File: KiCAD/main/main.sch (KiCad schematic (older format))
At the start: 14 parts, among them IC1 DHT22, J1 Charge controller, J2 Sound Sensor, J3 BuckConverter, J4 Anemometer, Q1 Q_NJFET_DGS, U1 4020, U1 4N25, U2 4N25

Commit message: alimentação através do micro
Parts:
- removed Q1: Q_NJFET_DGS, symbol Device:Q_NJFET_DGS
- removed R1: 1k, symbol Device:R
- removed R? (x2): R, Resistor_SMD:R_1206_3216Metric, symbol Device:R
- removed U2: 4N25, Package_DIP:DIP-6_W7.62mm, symbol Isolator:4N25
- added SW?: SW_DPDT_x2, symbol Switch:SW_DPDT_x2
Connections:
- net VDD_on is gone; now on net supply_on: IC1.1 (VDD), J2.3 (Pin_3)
- net Vin_Buck: now also SW?.1 (A); no longer J1.1 (Pin_1)
- new net: J1.1 (Pin_1), SW?.2 (B)
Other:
- moved on the sheet: IC1, J4
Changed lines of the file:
@@
 Text Label 2900 3450 2    50   ~ 0
 DHT22_Data
-Text Label 1550 2700 0    50   ~ 0
+Text Label 2450 2400 0    50   ~ 0
 Vin_Buck
 Text Label 1550 2800 0    50   ~ 0
@@
 	4750 2650 4450 2650
 Wire Wire Line
-	9100 2950 9500 2950
-Wire Wire Line
-	1200 3900 1500 3900
+	9250 2700 9650 2700
 $Comp
 L Connector_Generic:Conn_01x04 J3
@@
 	1200 1750 1500 1750
 Wire Wire Line
-	1550 2700 1250 2700
-Wire Wire Line
 	1550 2800 1250 2800
 $Comp
 L Connector_Generic:Conn_01x02 J4
 U 1 1 5FC61584
-P 9700 2850
-F 0 "J4" H 9780 2842 50  0000 L CNN
-F 1 "Anemometer" H 9780 2751 50  0000 L CNN
-F 2 "Connector_JST:JST_PH_B2B-PH-K_1x02_P2.00mm_Vertical" H 9700 2850 50  0001 C CNN
-F 3 "~" H 9700 2850 50  0001 C CNN
-	1    9700 2850
-	1    0    0    -1
-$EndComp
-Text Label 8800 4400 2    50   ~ 0
-GND
-Text Label 8800 4200 2    50   ~ 0
+P 9850 2600
+F 0 "J4" H 9930 2592 50  0000 L CNN
+F 1 "Anemometer" H 9930 2501 50  0000 L CNN
+F 2 "Connector_JST:JST_PH_B2B-PH-K_1x02_P2.00mm_Vertical" H 9850 2600 50  0001 C CNN
+F 3 "~" H 9850 2600 50  0001 C CNN
+	1    9850 2600
+	1    0    0    -1
+$EndComp
+Text Label 8150 3900 2    50   ~ 0
+GND
+Text Label 8150 3700 2    50   ~ 0
 DHT22_Data
 Wire Wire Line
-	9000 4300 8900 4300
-NoConn ~ 8900 4300
-Wire Wire Line
-	9000 4400 8800 4400
-Wire Wire Line
-	9000 4200 8800 4200
+	8350 3800 8250 3800
+NoConn ~ 8250 3800
+Wire Wire Line
+	8350 3900 8150 3900
+Wire Wire Line
+	8350 3700 8150 3700
 $Comp
 L DHT22:DHT22 IC1
 U 1 1 5FB3BE3A
-P 9000 4100
-F 0 "IC1" H 9342 3535 50  0000 C CNN
-F 1 "DHT22" H 9342 3626 50  0000 C CNN
-F 2 "DHT22" H 9750 4200 50  0001 L CNN
-F 3 "https://datasheet4u.com/datasheet-parts/DHT22-datasheet.php?id=792211" H 9750 4100 50  0001 L CNN
-F 4 "Digital-output relative humidity & temperature sensor/module DHT22" H 9750 4000 50  0001 L CNN "Description"
-F 5 "25.1" H 9750 3900 50  0001 L CNN "Height"
-F 6 "Aosong Electronics" H 9750 3800 50  0001 L CNN "Manufacturer_Name"
-F 7 "DHT22" H 9750 3700 50  0001 L CNN "Manufacturer_Part_Number"
-F 8 "" H 9750 3600 50  0001 L CNN "Arrow Part Number"
-F 9 "" H 9750 3500 50  0001 L CNN "Arrow Price/Stock"
-F 10 "" H 9750 3400 50  0001 L CNN "Mouser Part Number"
-F 11 "" H 9750 3300 50  0001 L CNN "Mouser Price/Stock"
-	1    9000 4100
+P 8350 3600
+F 0 "IC1" H 8692 3035 50  0000 C CNN
+F 1 "DHT22" H 8692 3126 50  0000 C CNN
+F 2 "DHT22" H 9100 3700 50  0001 L CNN
+F 3 "https://datasheet4u.com/datasheet-parts/DHT22-datasheet.php?id=792211" H 9100 3600 50  0001 L CNN
+F 4 "Digital-output relative humidity & temperature sensor/module DHT22" H 9100 3500 50  0001 L CNN "Description"
+F 5 "25.1" H 9100 3400 50  0001 L CNN "Height"
+F 6 "Aosong Electronics" H 9100 3300 50  0001 L CNN "Manufacturer_Name"
+F 7 "DHT22" H 9100 3200 50  0001 L CNN "Manufacturer_Part_Number"
+F 8 "" H 9100 3100 50  0001 L CNN "Arrow Part Number"
+F 9 "" H 9100 3000 50  0001 L CNN "Arrow Price/Stock"
+F 10 "" H 9100 2900 50  0001 L CNN "Mouser Part Number"
+F 11 "" H 9100 2800 50  0001 L CNN "Mouser Price/Stock"
+	1    8350 3600
 	1    0    0    -1
 $EndComp
@@
 supply_on
 Wire Wire Line
-	9100 3000 9100 2950
-Text Label 3550 900  2    50   ~ 0
-VDD
-Wire Wire Line
-	3550 1850 3550 2000
-Text Label 3550 2000 2    50   ~ 0
-GND
-$Comp
-L Device:R R?
-U 1 1 5FD2702C
-P 3550 1700
-F 0 "R?" H 3620 1746 50  0000 L CNN
-F 1 "R" H 3620 1655 50  0000 L CNN
-F 2 "Resistor_SMD:R_1206_3216Metric" V 3480 1700 50  0001 C CNN
-F 3 "~" H 3550 1700 50  0001 C CNN
-	1    3550 1700
-	-1   0    0    -1
-$EndComp
-Wire Wire Line
-	3550 1050 3550 900
-$Comp
-L Device:R R?
-U 1 1 5FD27024
-P 3100 1250
-F 0 "R?" H 3170 1296 50  0000 L CNN
-F 1 "R" H 3170 1205 50  0000 L CNN
-F 2 "Resistor_SMD:R_1206_3216Metric" V 3030 1250 50  0001 C CNN
-F 3 "~" H 3100 1250 50  0001 C CNN
-	1    3100 1250
-	0    -1   1    0
-$EndComp
-Text Label 2750 1250 2    50   ~ 0
-supply_on
-Wire Wire Line
-	2950 1250 2750 1250
-Text Label 9100 3000 2    50   ~ 0
+	9250 2750 9250 2700
+Text Label 9250 2750 2    50   ~ 0
 VDD
 Text Label 7150 3000 0    50   ~ 0
 GND
 Wire Wire Line
-	3550 1450 3550 1500
-Wire Wire Line
-	3550 1500 3850 1500
-Connection ~ 3550 1500
-Wire Wire Line
-	3550 1500 3550 1550
-Text Label 3850 1500 0    50   ~ 0
-VDD_on
-Wire Wire Line
 	1200 1950 1500 1950
 Text Label 1500 1950 0    50   ~ 0
-VDD_on
-Wire Wire Line
-	9000 4100 8800 4100
-Text Label 8800 4100 2    50   ~ 0
-VDD_on
-$Comp
-L Device:Q_NJFET_DGS Q1
-U 1 1 5FCA4F46
-P 3450 1250
-F 0 "Q1" H 3641 1296 50  0000 L CNN
-F 1 "Q_NJFET_DGS" H 3641 1205 50  0000 L CNN
-F 2 "" H 3650 1350 50  0001 C CNN
-F 3 "~" H 3450 1250 50  0001 C CNN
-	1    3450 1250
-	1    0    0    -1
-$EndComp
-Wire Wire Line
-	9100 2850 9500 2850
+supply_on
+Wire Wire Line
+	8350 3600 8150 3600
+Text Label 8150 3600 2    50   ~ 0
+supply_on
+Wire Wire Line
+	9250 2600 9650 2600
 Wire Wire Line
 	7200 2100 7200 2300
@@
 	-1   0    0    -1
 $EndComp
-Text Label 9100 2850 2    50   ~ 0
+Text Label 9250 2600 2    50   ~ 0
 Anemometer_Out
-Wire Wire Line
-	6050 1300 6050 1500
-Text Label 6050 1300 1    50   ~ 0
-VDD
-Text Label 4900 1400 2    50   ~ 0
-supply_on
-Wire Wire Line
-	5950 1500 6050 1500
-Wire Wire Line
-	5050 1400 4900 1400
-Text Label 5150 1600 2    50   ~ 0
-GND
-Wire Wire Line
-	5350 1600 5150 1600
-$Comp
-L Device:R R1
-U 1 1 5FCAEA05
-P 5200 1400
-F 0 "R1" V 4993 1400 50  0000 C CNN
-F 1 "1k" V 5084 1400 50  0000 C CNN
-F 2 "" V 5130 1400 50  0001 C CNN
-F 3 "~" H 5200 1400 50  0001 C CNN
-	1    5200 1400
-	0    -1   1    0
-$EndComp
-$Comp
-L Isolator:4N25 U2
-U 1 1 5FCAEA0B
-P 5650 1500
-F 0 "U2" H 5650 1825 50  0000 C CNN
-F 1 "4N25" H 5650 1734 50  0000 C CNN
-F 2 "Package_DIP:DIP-6_W7.62mm" H 5450 1300 50  0001 L CIN
-F 3 "https://www.vishay.com/docs/83725/4n25.pdf" H 5650 1500 50  0001 L CNN
-	1    5650 1500
-	1    0    0    -1
-$EndComp
-Wire Wire Line
-	5950 1600 6150 1600
-Text Label 6150 1600 0    50   ~ 0
-VDD_on
 Wire Wire Line
 	3200 3750 2900 3750
@@
 Text Label 1550 2900 0    50   ~ 0
 Battery_status
+$Comp
+L Switch:SW_DPDT_x2 SW?
+U 1 1 5FCD740E
+P 2100 2500
+F 0 "SW?" H 2100 2785 50  0000 C CNN
+F 1 "SW_DPDT_x2" H 2100 2694 50  0000 C CNN
+F 2 "" H 2100 2500 50  0001 C CNN
+F 3 "~" H 2100 2500 50  0001 C CNN
+	1    2100 2500
+	1    0    0    -1
+$EndComp
+Wire Wire Line
+	1200 3900 1500 3900
+Wire Wire Line
+	2300 2400 2450 2400
+Wire Wire Line
+	1900 2700 1900 2500
+Wire Wire Line
+	1250 2700 1900 2700
 $EndSCHEMATC

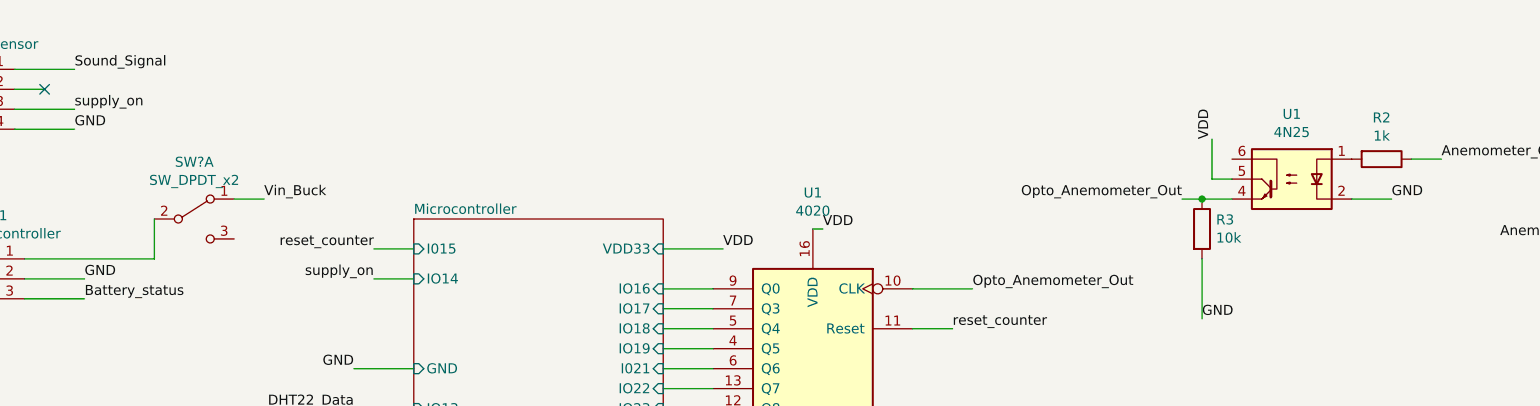
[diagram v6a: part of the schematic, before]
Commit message: troca do DPDT por um SPDT
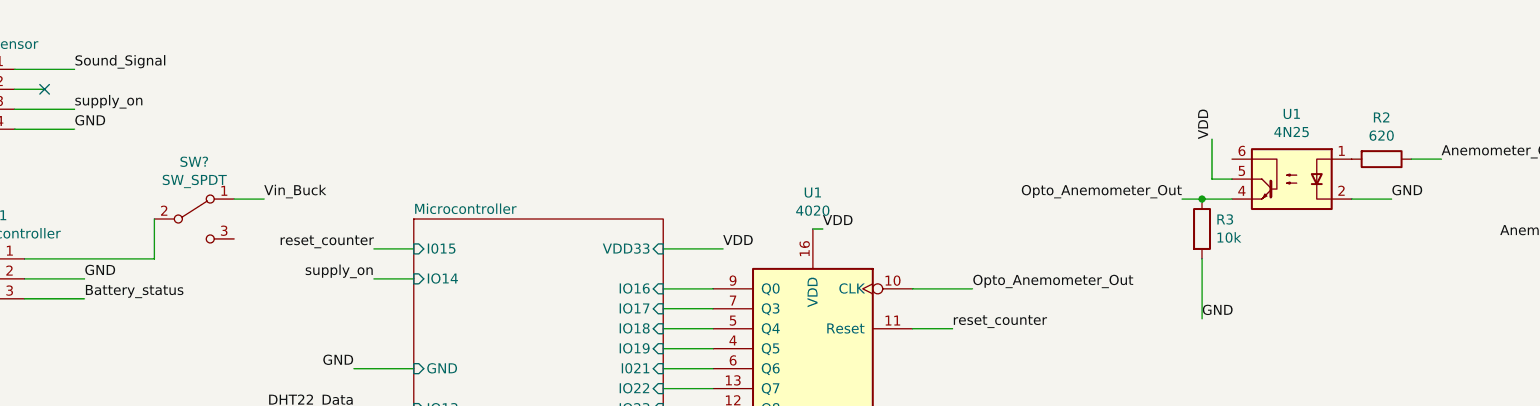
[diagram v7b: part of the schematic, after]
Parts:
- removed SW?: SW_DPDT_x2, symbol Switch:SW_DPDT_x2
- added SW?: SW_SPDT, symbol Switch:SW_SPDT
- R2: value 1k -> 620
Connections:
- net Vin_Buck: now also SW?.1 (A)
- net at J1.1 (Pin_1): now also SW?.2 (B)
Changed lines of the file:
@@
 P 8050 2200
 F 0 "R2" V 7843 2200 50  0000 C CNN
-F 1 "1k" V 7934 2200 50  0000 C CNN
+F 1 "620" V 7934 2200 50  0000 C CNN
 F 2 "" V 7980 2200 50  0001 C CNN
 F 3 "~" H 8050 2200 50  0001 C CNN
@@
 Text Label 1550 2900 0    50   ~ 0
 Battery_status
-$Comp
-L Switch:SW_DPDT_x2 SW?
-U 1 1 5FCD740E
-P 2100 2500
-F 0 "SW?" H 2100 2785 50  0000 C CNN
-F 1 "SW_DPDT_x2" H 2100 2694 50  0000 C CNN
-F 2 "" H 2100 2500 50  0001 C CNN
-F 3 "~" H 2100 2500 50  0001 C CNN
-	1    2100 2500
-	1    0    0    -1
-$EndComp
 Wire Wire Line
 	1200 3900 1500 3900
@@
 Wire Wire Line
 	1250 2700 1900 2700
+$Comp
+L Switch:SW_SPDT SW?
+U 1 1 5FCD21D1
+P 2100 2500
+F 0 "SW?" H 2100 2785 50  0000 C CNN
+F 1 "SW_SPDT" H 2100 2694 50  0000 C CNN
+F 2 "" H 2100 2500 50  0001 C CNN
+F 3 "~" H 2100 2500 50  0001 C CNN
+	1    2100 2500
+	1    0    0    -1
+$EndComp
 $EndSCHEMATC

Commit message: Fix footprints
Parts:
- R2: footprint (none) -> Resistor_SMD:R_1206_3216Metric
- SW?: footprint (none) -> Button_Switch_THT:SW_CuK_OS102011MA1QN1_SPDT_Angled
- U1: footprint Package_DIP:DIP-6_W7.62mm -> Package_DIP:DIP-6_W7.62mm_LongPads
- U1: footprint (none) -> Package_DIP:DIP-16_W7.62mm_LongPads
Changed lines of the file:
@@
 F 0 "U1" H 5200 4331 50  0000 C CNN
 F 1 "4020" H 5200 4240 50  0000 C CNN
-F 2 "" H 5200 3350 50  0001 C CNN
+F 2 "Package_DIP:DIP-16_W7.62mm_LongPads" H 5200 3350 50  0001 C CNN
 F 3 "http://www.intersil.com/content/dam/Intersil/documents/cd40/cd4020bms-24bms-40bms.pdf" H 5200 3350 50  0001 C CNN
 	1    5200 3350
@@
 F 0 "R2" V 7843 2200 50  0000 C CNN
 F 1 "620" V 7934 2200 50  0000 C CNN
-F 2 "" V 7980 2200 50  0001 C CNN
+F 2 "Resistor_SMD:R_1206_3216Metric" V 7980 2200 50  0001 C CNN
 F 3 "~" H 8050 2200 50  0001 C CNN
 	1    8050 2200
@@
 F 0 "U1" H 7600 2625 50  0000 C CNN
 F 1 "4N25" H 7600 2534 50  0000 C CNN
-F 2 "Package_DIP:DIP-6_W7.62mm" H 7400 2100 50  0001 L CIN
+F 2 "Package_DIP:DIP-6_W7.62mm_LongPads" H 7400 2100 50  0001 L CIN
 F 3 "https://www.vishay.com/docs/83725/4n25.pdf" H 7600 2300 50  0001 L CNN
 	1    7600 2300
@@
 F 0 "SW?" H 2100 2785 50  0000 C CNN
 F 1 "SW_SPDT" H 2100 2694 50  0000 C CNN
-F 2 "" H 2100 2500 50  0001 C CNN
+F 2 "Button_Switch_THT:SW_CuK_OS102011MA1QN1_SPDT_Angled" H 2100 2500 50  0001 C CNN
 F 3 "~" H 2100 2500 50  0001 C CNN
 	1    2100 2500
